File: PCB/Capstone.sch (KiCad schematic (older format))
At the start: 0 parts

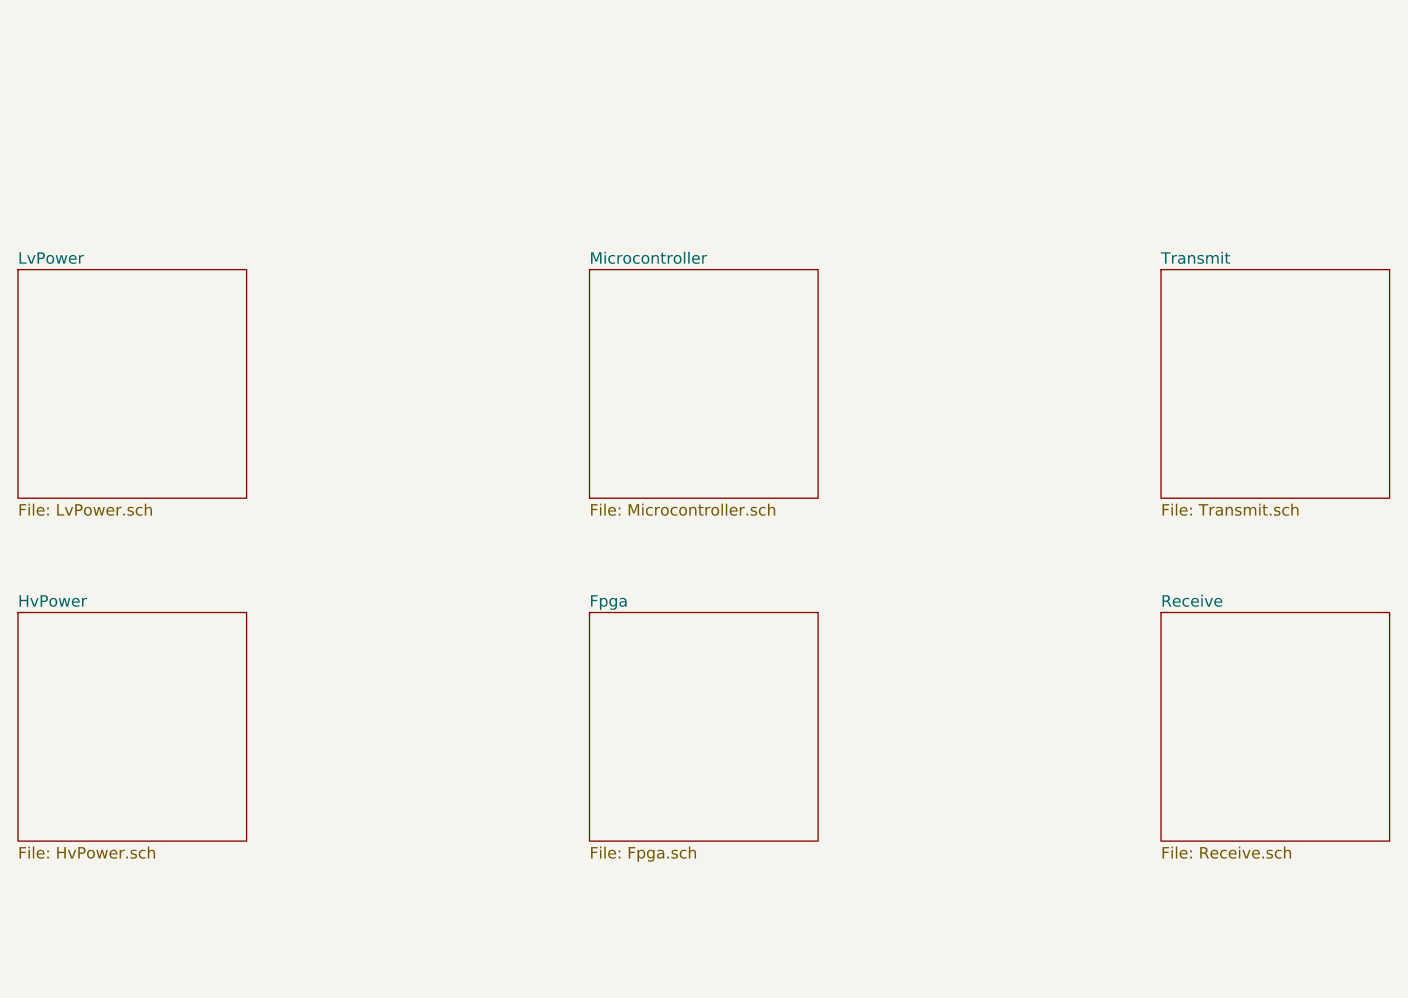
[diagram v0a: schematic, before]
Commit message: Add diode pair to library
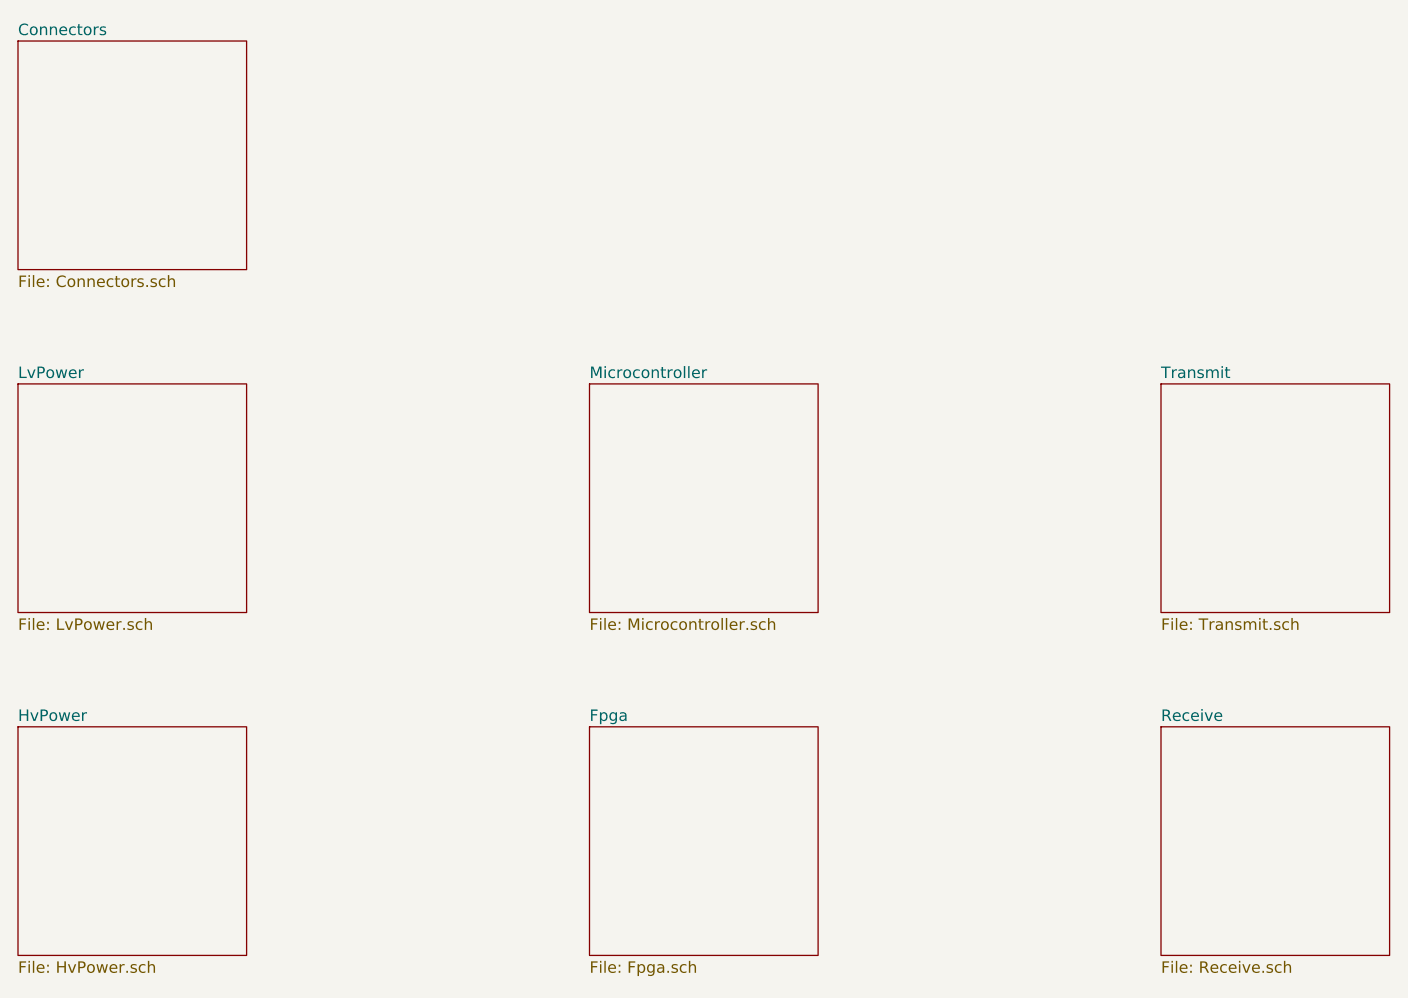
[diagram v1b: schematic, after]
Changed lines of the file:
@@
 $Descr A4 11693 8268
 encoding utf-8
-Sheet 1 7
+Sheet 1 8
 Title ""
 Date ""
@@
 $EndDescr
 $Sheet
-S 1000 2500 1000 1000
+S 1000 3000 1000 1000
 U 5DCDE8BF
 F0 "LvPower" 50
@@
 $EndSheet
 $Sheet
-S 3500 2500 1000 1000
+S 3500 3000 1000 1000
 U 5DCDE970
 F0 "Microcontroller" 50
@@
 $EndSheet
 $Sheet
-S 1000 4000 1000 1000
+S 1000 4500 1000 1000
 U 5DCDEA18
 F0 "HvPower" 50
@@
 $EndSheet
 $Sheet
-S 3500 4000 1000 1000
+S 3500 4500 1000 1000
 U 5DCDEC3D
 F0 "Fpga" 50
@@
 $EndSheet
 $Sheet
-S 6000 2500 1000 1000
+S 6000 3000 1000 1000
 U 5DCDED08
 F0 "Transmit" 50
@@
 $EndSheet
 $Sheet
-S 6000 4000 1000 1000
+S 6000 4500 1000 1000
 U 5DCDEDA5
 F0 "Receive" 50
 F1 "Receive.sch" 50
 $EndSheet
+$Sheet
+S 1000 1500 1000 1000
+U 5DCE3F32
+F0 "Connectors" 50
+F1 "Connectors.sch" 50
+$EndSheet
 $EndSCHEMATC
